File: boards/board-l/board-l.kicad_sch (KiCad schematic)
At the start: 73 parts, among them J2 2.54mm 1x6 female, J3 SWD 1x5 (hand-fit), J4 UART pads, J5 Power switch solder pads, SW1 EC11 15-detent, SW2 WR11AS (panel rocker), U2 AL8860MP-13, U3 STM32G031F8P6, U4 AP63203WU-7

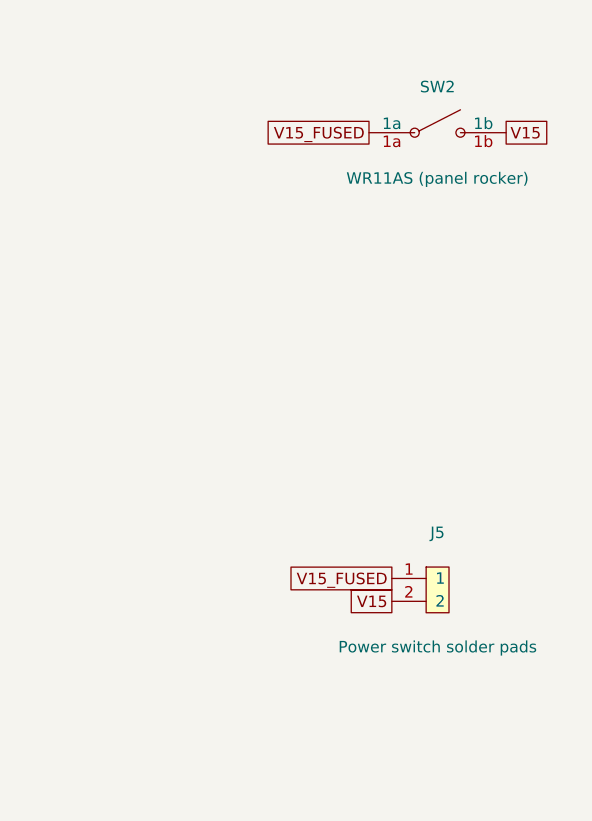
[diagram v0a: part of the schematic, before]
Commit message: Replace external rocker schematic with JLCPCB C496154 and audited slotted assets
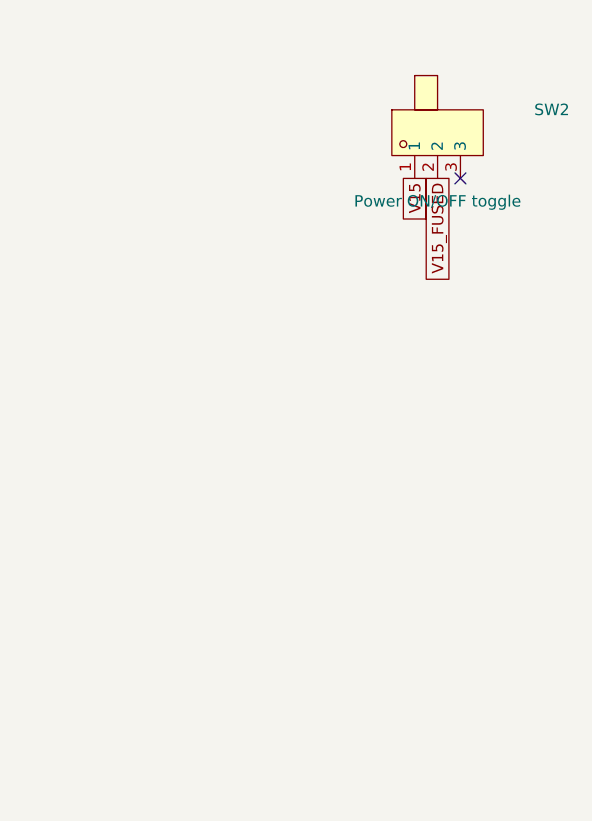
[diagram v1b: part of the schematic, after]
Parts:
- removed J5: Power switch solder pads, zudo-led-lamp:SolderWire_1x02_P5.08mm, symbol zudo-led-lamp:Conn_1x02
- SW2: value WR11AS (panel rocker) -> Power ON/OFF toggle; footprint (none) -> zudo-led-lamp:SW-TH_1MS1T1B1M1QES-5; symbol zudo-led-lamp:WR11AS -> zudo-led-lamp:1MS1T1B1M1QES-5; Assembly External panel mount; hand wire via J5 -> (none); LCSC (none) -> C496154; MPN WR11AS -> (none); Manufacturer NKK Switches -> (none); Supplier DigiKey -> (none); Supplier Part 360-1507-ND -> (none)
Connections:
- net V15: now also SW2.1; no longer SW2.1b
- net V15_FUSED: now also SW2.2; no longer SW2.1a
- no-connect marks 11 -> 12
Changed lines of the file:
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@@
 	(paper "A2")
 	(symbol
-		(lib_id "zudo-led-lamp:WR11AS")
+		(lib_id "zudo-led-lamp:1MS1T1B1M1QES-5")
 		(at 444.5 50.8 0)
 		(unit 1)
 		(exclude_from_sim no)
 		(in_bom yes)
-		(on_board no)
+		(on_board yes)
 		(dnp no)
 		(property "Reference" "SW2"
-			(at 444.5 45.72 0)
+			(at 457.2 48.26 0)
 			(effects
 				(font (size 1.27 1.27))
 			)
 		)
-		(property "Value" "WR11AS (panel rocker)"
-			(at 444.5 55.88 0)
+		(property "Value" "Power ON/OFF toggle"
+			(at 444.5 58.42 0)
 			(effects
 				(font (size 1.27 1.27))
 			)
 		)
-		(property "Footprint" ""
+		(property "Footprint" "zudo-led-lamp:SW-TH_1MS1T1B1M1QES-5"
 			(at 444.5 50.8 0)
 			(effects
@@
 			)
 		)
-		(property "Datasheet" "https://www.nkkswitches.com/pdf/WR.pdf"
-			(at 444.5 50.8 0)
-			(effects
-				(font (size 1.27 1.27))
-				(hide yes)
-			)
-		)
-		(property "MPN" "WR11AS"
-			(at 444.5 50.8 0)
-			(effects
-				(font (size 1.27 1.27))
-				(hide yes)
-			)
-		)
-		(property "Manufacturer" "NKK Switches"
-			(at 444.5 50.8 0)
-			(effects
-				(font (size 1.27 1.27))
-				(hide yes)
-			)
-		)
-		(property "Supplier" "DigiKey"
-			(at 444.5 50.8 0)
-			(effects
-				(font (size 1.27 1.27))
-				(hide yes)
-			)
-		)
-		(property "Supplier Part" "360-1507-ND"
-			(at 444.5 50.8 0)
-			(effects
-				(font (size 1.27 1.27))
-				(hide yes)
-			)
-		)
-		(property "Assembly" "External panel mount; hand wire via J5"
+		(property "Datasheet" ""
 			(at 444.5 50.8 0)
 			(effects
@@
 			)
 		)
-		(pin "1a"
-		)
-		(pin "1b"
-		)
-		(instances
-			(project "board-l"
-				(path "/ef98bbc0-7939-597a-8146-6f278c102a15"
-					(reference "SW2")
-					(unit 1)
-				)
-			)
-		)
-	)
-	(symbol
-		(lib_id "zudo-led-lamp:Conn_1x02")
-		(at 444.5 101.6 0)
-		(unit 1)
-		(exclude_from_sim no)
-		(in_bom no)
-		(on_board yes)
-		(dnp no)
-		(property "Reference" "J5"
-			(at 444.5 95.25 0)
-			(effects
-				(font (size 1.27 1.27))
-			)
-		)
-		(property "Value" "Power switch solder pads"
-			(at 444.5 107.95 0)
-			(effects
-				(font (size 1.27 1.27))
-			)
-		)
-		(property "Footprint" "zudo-led-lamp:SolderWire_1x02_P5.08mm"
-			(at 444.5 101.6 0)
-			(effects
-				(font (size 1.27 1.27))
-				(hide yes)
-			)
-		)
-		(property "Datasheet" ""
-			(at 444.5 101.6 0)
+		(property "LCSC" "C496154"
+			(at 444.5 58.42 0)
 			(effects
 				(font (size 1.27 1.27))
@@
 		(pin "2"
 		)
+		(pin "3"
+		)
 		(instances
 			(project "board-l"
 				(path "/ef98bbc0-7939-597a-8146-6f278c102a15"
-					(reference "J5")
+					(reference "SW2")
 					(unit 1)
 				)
@@
 	(global_label "V15_FUSED"
 		(shape passive)
-		(at 439.42 100.33 180)
-		(effects
-			(font (size 1.27 1.27))
-			(justify right)
-		)
-	)
-	(global_label "V15_FUSED"
-		(shape passive)
-		(at 436.88 50.8 180)
+		(at 444.5 55.88 270)
 		(effects
 			(font (size 1.27 1.27))
@@
 	(global_label "V15"
 		(shape passive)
-		(at 452.12 50.8 0)
-		(effects
-			(font (size 1.27 1.27))
-			(justify left)
-		)
-	)
-	(global_label "V15"
-		(shape passive)
-		(at 439.42 102.87 180)
+		(at 441.96 55.88 270)
 		(effects
 			(font (size 1.27 1.27))
@@
 	)
 	(no_connect
+		(at 447.04 55.88)
+	)
+	(no_connect

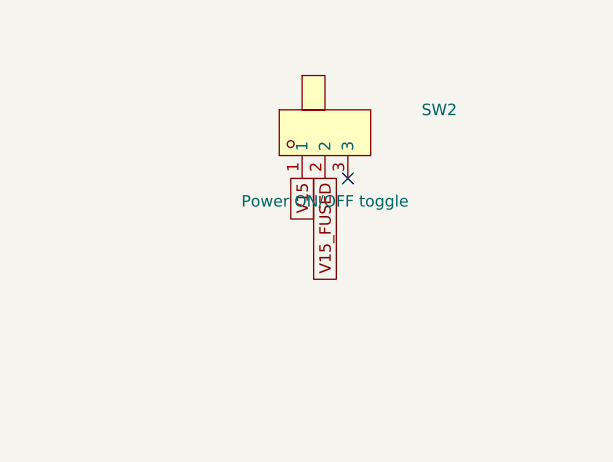
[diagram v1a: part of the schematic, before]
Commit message: Place and route rear C496154 switch clear of the stacked power board
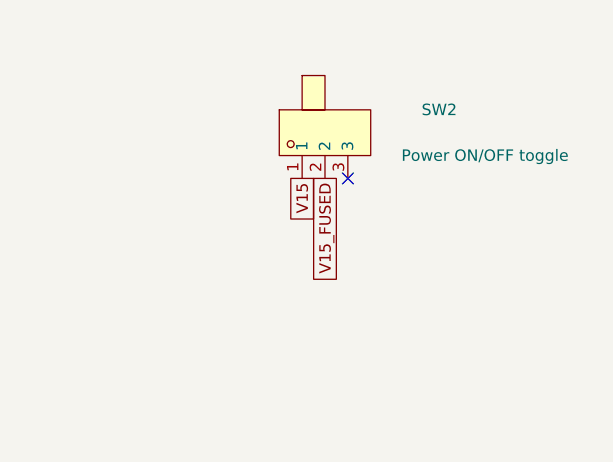
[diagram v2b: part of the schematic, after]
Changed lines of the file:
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@@
 		)
 		(property "Value" "Power ON/OFF toggle"
-			(at 444.5 58.42 0)
+			(at 462.28 53.34 0)
 			(effects
 				(font (size 1.27 1.27))

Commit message: feat: replace tall controls with stopped ALPS pot and short slider
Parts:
- removed C23: 100nF/50V, zudo-led-lamp:C0603, symbol zudo-led-lamp:CC0603KRX7R9BB104
- removed R23: 10k, zudo-led-lamp:R0805, symbol zudo-led-lamp:0805W8F1002T5E
- removed R28: 100R, zudo-led-lamp:R0603, symbol zudo-led-lamp:0603WAF1000T5E
- removed SW1: EC11 15-detent, zudo-led-lamp:SW-TH_ALPS_EC11L1525G01, symbol zudo-led-lamp:EC11L1525G01
- added RV1: 10k brightness pot, zudo-led-lamp:POT-TH_RK10J11E0034, symbol zudo-led-lamp:RK10J11E0034
- R22: value 10k -> 100k wiper pull-down; footprint zudo-led-lamp:R0805 -> zudo-led-lamp:R0603; symbol zudo-led-lamp:0805W8F1002T5E -> zudo-led-lamp:0603WAF1003T5E; LCSC C17414 -> C25803
- SW2: value Power ON/OFF toggle -> Power ON/OFF slide; footprint zudo-led-lamp:SW-TH_1MS1T1B1M1QES-5 -> zudo-led-lamp:SW-TH_SS-12D01-G020; symbol zudo-led-lamp:1MS1T1B1M1QES-5 -> zudo-led-lamp:SS-12D01-G020; LCSC C496154 -> C5446803
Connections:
- net GND: now also R22.2, RV1.1 (LOW)
- net V3P3: now also RV1.3 (HIGH); no longer R22.1
- net ENC_A renamed BRIGHT_ADC
- net BRIGHT_ADC: now also R22.1; no longer R22.2
- net ENC_A_SW renamed BRIGHT_WIPER
- net BRIGHT_WIPER: now also RV1.2 (WIPER)
- net ENC_B: no longer names the net of U3.8 (PA1)
- no-connect marks 12 -> 15
